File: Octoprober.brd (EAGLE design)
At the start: 130.8 x 91.7 mm, 135 parts, among them J1 10118193-0001LF, J2 26-60-4020, P1 TC33X-1, SW1 101-0134-EV, SW2 EVQ-Q2203W, SW3 EVQ-Q2203W, SW4 EVQ-Q2203W, SW5 EVQ-Q2203W, U1 P8X32A-M44, U10 MAX31855KASA+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

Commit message: Finished REV0.
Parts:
- added U$3, U$4, U$5, U$6: (no value), PP_Connectors:MOUNT_HOLE_2.8MM
- BATT1: value 1042 -> (none); device PP_Connectors:KEYSTONE_1042 -> PP_Connectors:HEADER_01X02_PTH
- L1: device PP_Passives:0603@1 -> PP_Passives:0603
- moved BATT1 33.1 mm to (80.8, 6.60), flipped to the top, turned to 0 degrees
- moved U$1 10.3 mm to (96.8, 68.6)
- moved U$2 6.43 mm to (0.51, 7.11)
- moved C1 2.96 mm to (115.8, 19.6)
- moved R2 2.96 mm to (109.0, 19.6)
- moved R3 2.96 mm to (111.3, 19.6)
- moved R4 2.96 mm to (113.5, 19.6)
- moved R5 2.96 mm to (118.1, 19.6)
- moved R6 2.96 mm to (120.4, 19.6)
- moved R7 2.96 mm to (122.7, 19.6)
- moved SD1 2.96 mm to (119.1, 4.57)
- moved R18 0.13 mm to (53.1, 18.4)
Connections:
- net GND: now also BATT1.1; no longer BATT1.N
- net VBATT: now also BATT1.2; no longer BATT1.P
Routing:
- net GND: track 376.6 -> 369.3 mm, vias 57 -> 56
- net VBATT: track 45.4 -> 43.2 mm
- net SD_CS: track 47.6 -> 49.6 mm
- net SD_SCLK: track 45.1 -> 47.2 mm
- net SD_DI: track 47.3 -> 49.4 mm
- net SD_DO: track 46.0 -> 47.6 mm
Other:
- outline, holes or cut-outs redrawn
- board text added: "+V"
- board text added: "GND"
- board text added: "PWR"
- board text added: "RESET"
- board text added: "TX/RX"

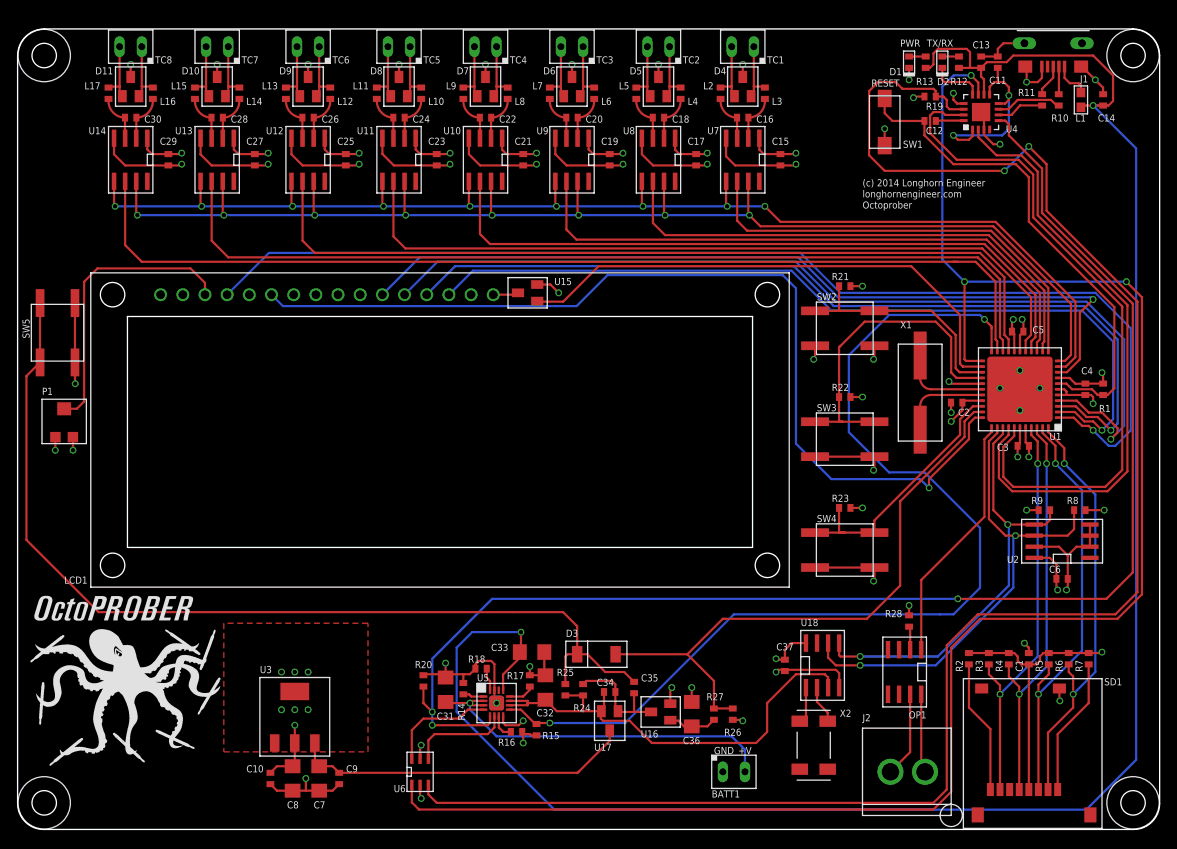
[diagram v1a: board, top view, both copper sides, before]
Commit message: Added ADC MCP3021 to monitor battery
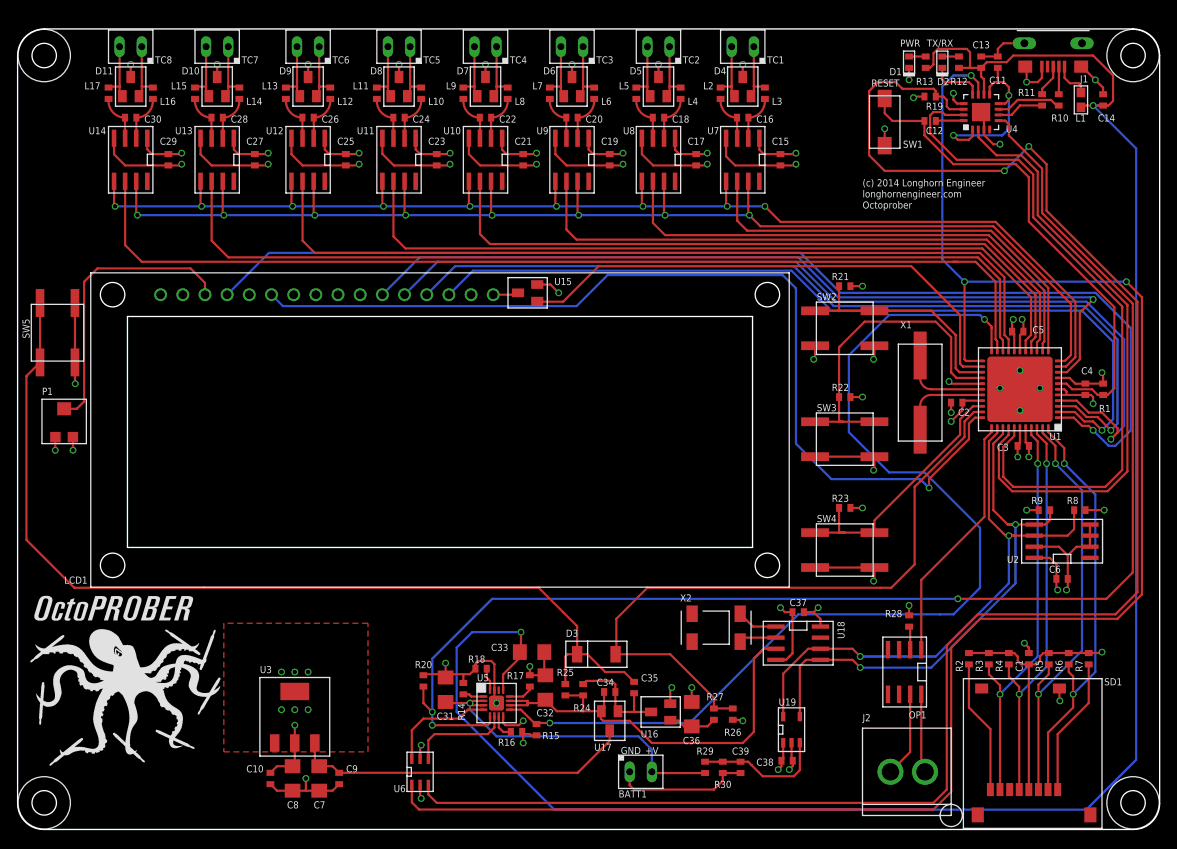
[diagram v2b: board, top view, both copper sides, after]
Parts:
- added C38, C39: 0.1uF, PP_Passives:0402
- added R29: 100K, PP_Passives:0402
- added R30: 254K, PP_Passives:0402
- added U19: MCP3021A5T-E/OT, PP_DigitalIC:SOT-23A
- moved X2 17.5 mm to (80.0, 23.1), turned to 180 degrees
- moved BATT1 10.7 mm to (70.1, 6.60)
- moved C37 6.28 mm to (89.4, 24.9), turned to 180 degrees
- moved U18 3.78 mm to (89.4, 21.3), turned to 270 degrees
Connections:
- new net A_0: C39.1, R29.2, R30.1, U19.3
- net 3.3V: now also C38.1, U19.1
- net GND: now also C38.2, C39.2, R30.2, U19.2
- net SCL: now also U19.5
- net SDA: now also U19.4
- net VBATT: now also R29.1
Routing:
- net GND: track 369.3 -> 388.2 mm, vias 56 -> 57
- net A_0: track 0.00 -> 15.2 mm
- net SDA: track 49.8 -> 61.2 mm
- net PWR_SW: track 69.8 -> 78.8 mm
- net SCL: track 57.0 -> 65.7 mm
- net VBATT: track 43.2 -> 38.6 mm
- net 3.3V: track 253.7 -> 257.7 mm, vias 27 -> 28
- net SYS_V: track 54.6 -> 51.4 mm

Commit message: Added part values and created BOM.txt
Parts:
- OP1: value (none) -> ACPL-227
- U4: value (none) -> FT230XQ-R
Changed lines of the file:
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@@
 <?xml version="1.0" encoding="utf-8"?>
 <!DOCTYPE eagle SYSTEM "eagle.dtd">
-<eagle version="6.3">
+<eagle version="6.5.0">
 <drawing>
 <settings>
@@
 <attribute name="NAME" x="121.166" y="81.08" size="0.8128" layer="25" font="vector"/>
 </element>
-<element name="U4" library="PP_DigitalIC" package="QFN-16" value="" x="110.363" y="82.169" smashed="yes" rot="R90">
+<element name="U4" library="PP_DigitalIC" package="QFN-16" value="FT230XQ-R" x="110.363" y="82.169" smashed="yes" rot="R90">
 <attribute name="NAME" x="113.189" y="79.835" size="0.8128" layer="25" font="vector"/>
 </element>
@@
 <element name="U$2" library="PP_Aesthetics" package="OCTOPROBER_LOGO" value="OCTOPROBER_LOGONORMAL" x="0.508" y="7.112"/>
 <element name="J2" library="PP_Connectors" package="MOLEX_KK_2" value="26-60-4020" x="101.854" y="6.604"/>
-<element name="OP1" library="PP_DigitalIC" package="SOIC-8" value="" x="101.6" y="18.034" rot="R180"/>
+<element name="OP1" library="PP_DigitalIC" package="SOIC-8" value="ACPL-227" x="101.6" y="18.034" rot="R180"/>
 <element name="R28" library="PP_Passives" package="0402" value="120" x="102.108" y="23.876" smashed="yes" rot="R270">
 <attribute name="NAME" x="99.349" y="24.3205" size="0.8128" layer="25" font="vector"/>

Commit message: Fixed some part numbers
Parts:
- P1: value TC33X-1 -> TC33X-2-103E
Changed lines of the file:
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@@
 <attribute name="NAME" x="5.334" y="28.154" size="0.8128" layer="25" font="vector"/>
 </element>
-<element name="P1" library="PP_Passives" package="TC33_TRIMMER" value="TC33X-1" x="5.334" y="46.736" smashed="yes">
+<element name="P1" library="PP_Passives" package="TC33_TRIMMER" value="TC33X-2-103E" x="5.334" y="46.736" smashed="yes">
 <attribute name="NAME" x="2.794" y="49.784" size="0.8128" layer="25" font="vector"/>
 </element>

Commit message: Finished BOM...I hope.
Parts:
- BATT1: value (none) -> MIKROE-1120
- TC1, TC2, TC3, TC4, TC5, TC6, TC7, TC8: value (none) -> 282834-2
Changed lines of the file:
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@@
 <attribute name="NAME" x="99.349" y="24.3205" size="0.8128" layer="25" font="vector"/>
 </element>
-<element name="TC1" library="PP_Connectors" package="HEADER_01X02_PTH" value="" x="84.328" y="89.662" smashed="yes" rot="R180">
+<element name="TC1" library="PP_Connectors" package="HEADER_01X02_PTH" value="282834-2" x="84.328" y="89.662" smashed="yes" rot="R180">
 <attribute name="NAME" x="85.852" y="87.738" size="0.8128" layer="21" font="vector"/>
 </element>
-<element name="TC2" library="PP_Connectors" package="HEADER_01X02_PTH" value="" x="74.676" y="89.662" smashed="yes" rot="R180">
+<element name="TC2" library="PP_Connectors" package="HEADER_01X02_PTH" value="282834-2" x="74.676" y="89.662" smashed="yes" rot="R180">
 <attribute name="NAME" x="76.2" y="87.738" size="0.8128" layer="21" font="vector"/>
 </element>
-<element name="TC3" library="PP_Connectors" package="HEADER_01X02_PTH" value="" x="64.77" y="89.662" smashed="yes" rot="R180">
+<element name="TC3" library="PP_Connectors" package="HEADER_01X02_PTH" value="282834-2" x="64.77" y="89.662" smashed="yes" rot="R180">
 <attribute name="NAME" x="66.294" y="87.738" size="0.8128" layer="21" font="vector"/>
 </element>
-<element name="TC4" library="PP_Connectors" package="HEADER_01X02_PTH" value="" x="54.864" y="89.662" smashed="yes" rot="R180">
+<element name="TC4" library="PP_Connectors" package="HEADER_01X02_PTH" value="282834-2" x="54.864" y="89.662" smashed="yes" rot="R180">
 <attribute name="NAME" x="56.388" y="87.738" size="0.8128" layer="21" font="vector"/>
 </element>
-<element name="TC5" library="PP_Connectors" package="HEADER_01X02_PTH" value="" x="44.958" y="89.662" smashed="yes" rot="R180">
+<element name="TC5" library="PP_Connectors" package="HEADER_01X02_PTH" value="282834-2" x="44.958" y="89.662" smashed="yes" rot="R180">
 <attribute name="NAME" x="46.482" y="87.738" size="0.8128" layer="21" font="vector"/>
 </element>
-<element name="TC6" library="PP_Connectors" package="HEADER_01X02_PTH" value="" x="34.544" y="89.662" smashed="yes" rot="R180">
+<element name="TC6" library="PP_Connectors" package="HEADER_01X02_PTH" value="282834-2" x="34.544" y="89.662" smashed="yes" rot="R180">
 <attribute name="NAME" x="36.068" y="87.738" size="0.8128" layer="21" font="vector"/>
 </element>
-<element name="TC7" library="PP_Connectors" package="HEADER_01X02_PTH" value="" x="24.13" y="89.662" smashed="yes" rot="R180">
+<element name="TC7" library="PP_Connectors" package="HEADER_01X02_PTH" value="282834-2" x="24.13" y="89.662" smashed="yes" rot="R180">
 <attribute name="NAME" x="25.654" y="87.738" size="0.8128" layer="21" font="vector"/>
 </element>
-<element name="TC8" library="PP_Connectors" package="HEADER_01X02_PTH" value="" x="14.224" y="89.662" smashed="yes" rot="R180">
+<element name="TC8" library="PP_Connectors" package="HEADER_01X02_PTH" value="282834-2" x="14.224" y="89.662" smashed="yes" rot="R180">
 <attribute name="NAME" x="15.748" y="87.738" size="0.8128" layer="21" font="vector"/>
 </element>
@@
 <attribute name="NAME" x="8.89" y="86.487" size="0.8128" layer="25" font="vector"/>
 </element>
-<element name="BATT1" library="PP_Connectors" package="HEADER_01X02_PTH" value="" x="70.104" y="6.604"/>
+<element name="BATT1" library="PP_Connectors" package="HEADER_01X02_PTH" value="MIKROE-1120" x="70.104" y="6.604"/>
 <element name="U$3" library="PP_Connectors" package="MOUNT_HOLE_2.8MM" value="" x="3.048" y="88.646"/>
 <element name="U$4" library="PP_Connectors" package="MOUNT_HOLE_2.8MM" value="" x="127.762" y="88.646"/>

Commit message: Swapped VCC and VDD on display
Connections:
- net 3.3V: now also LCD1.2; no longer LCD1.1
- net GND: now also LCD1.1; no longer LCD1.2
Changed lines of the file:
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@@
 </element>
 <element name="U$1" library="PP_Aesthetics" package="LHE_FRAME" value="LHE_FRAME" x="96.774" y="68.58">
-<attribute name="REVNUM" value="REV 0" x="162.814" y="-19.05" size="1.778" layer="27" display="off"/>
+<attribute name="REVNUM" value="REV 1" x="162.814" y="-19.05" size="1.778" layer="27" display="off"/>
 <attribute name="DNAME" value="Parker Dillmann" x="162.814" y="-19.05" size="1.778" layer="27" display="off"/>
 </element>
@@
 <contactref element="C13" pad="2"/>
 <contactref element="C14" pad="2"/>
-<contactref element="LCD1" pad="2"/>
 <contactref element="LCD1" pad="5"/>
 <contactref element="P1" pad="3"/>
@@
 <via x="88.392" y="6.858" extent="1-16" drill="0.5"/>
 <wire x1="88.392" y1="6.858" x2="87.884" y2="6.858" width="0.254" layer="2"/>
+<contactref element="LCD1" pad="1"/>
 </signal>
 <signal name="RES">
@@
 <contactref element="C10" pad="1"/>
 <contactref element="C8" pad="1"/>
-<contactref element="LCD1" pad="1"/>
-<contactref element="P1" pad="1"/>
 <contactref element="C15" pad="1"/>
 <contactref element="U7" pad="4"/>
@@
 <wire x1="124.206" y1="52.324" x2="123.952" y2="52.324" width="0.254" layer="15"/>
 <wire x1="122.301" y1="51.069" x2="124.333" y2="51.069" width="0.254" layer="1"/>
-<wire x1="4.334" y1="44.936" x2="4.318" y2="44.92" width="0.254" layer="1"/>
-<wire x1="4.318" y1="44.92" x2="4.318" y2="43.434" width="0.254" layer="1"/>
-<via x="4.318" y="43.434" extent="1-16" drill="0.5"/>
-<wire x1="4.318" y1="43.434" x2="4.318" y2="42.926" width="0.254" layer="15"/>
 <wire x1="122.316" y1="36.576" x2="124.46" y2="36.576" width="0.254" layer="1"/>
 <via x="124.46" y="36.576" extent="1-16" drill="0.5"/>
@@
 <wire x1="87.122" y1="6.858" x2="86.36" y2="6.858" width="0.254" layer="15"/>
 <wire x1="87.488" y1="7.874" x2="87.696" y2="8.082" width="0.254" layer="1"/>
+<contactref element="LCD1" pad="2"/>
+<contactref element="P1" pad="1"/>
+<wire x1="4.334" y1="44.936" x2="4.318" y2="44.92" width="0.254" layer="1"/>
+<wire x1="4.318" y1="44.92" x2="4.318" y2="43.434" width="0.254" layer="1"/>
+<via x="4.318" y="43.434" extent="1-16" drill="0.5"/>
+<wire x1="4.318" y1="43.434" x2="4.318" y2="42.926" width="0.254" layer="15"/>
 </signal>
 <signal name="SD_RW">
